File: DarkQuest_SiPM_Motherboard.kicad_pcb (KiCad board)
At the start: 2 copper layers, 100 x 100 mm, 14 parts, among them J1 RJ45_Shielded, J2 SiPM Header, J3 SiPM Header, J4 SiPM Header, J5 SiPM Header

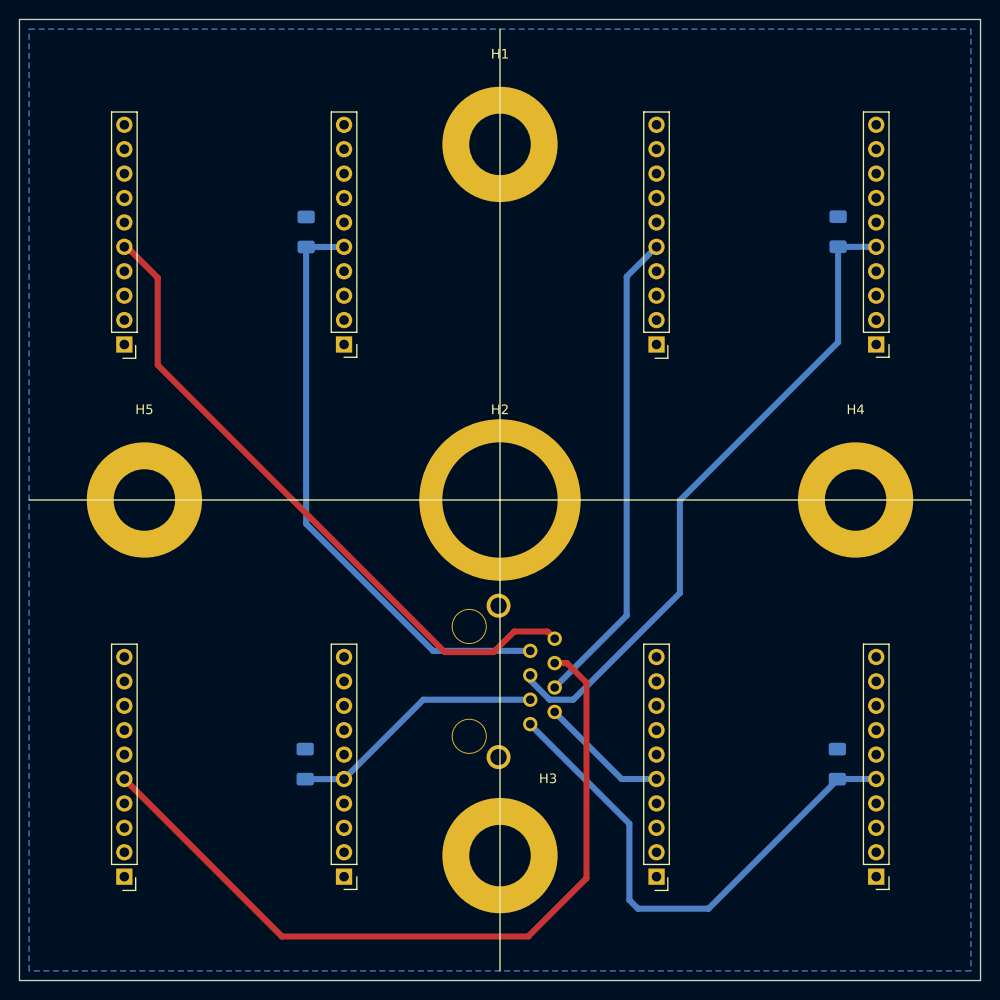
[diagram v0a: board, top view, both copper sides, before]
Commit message: Dual RJ45 Solution
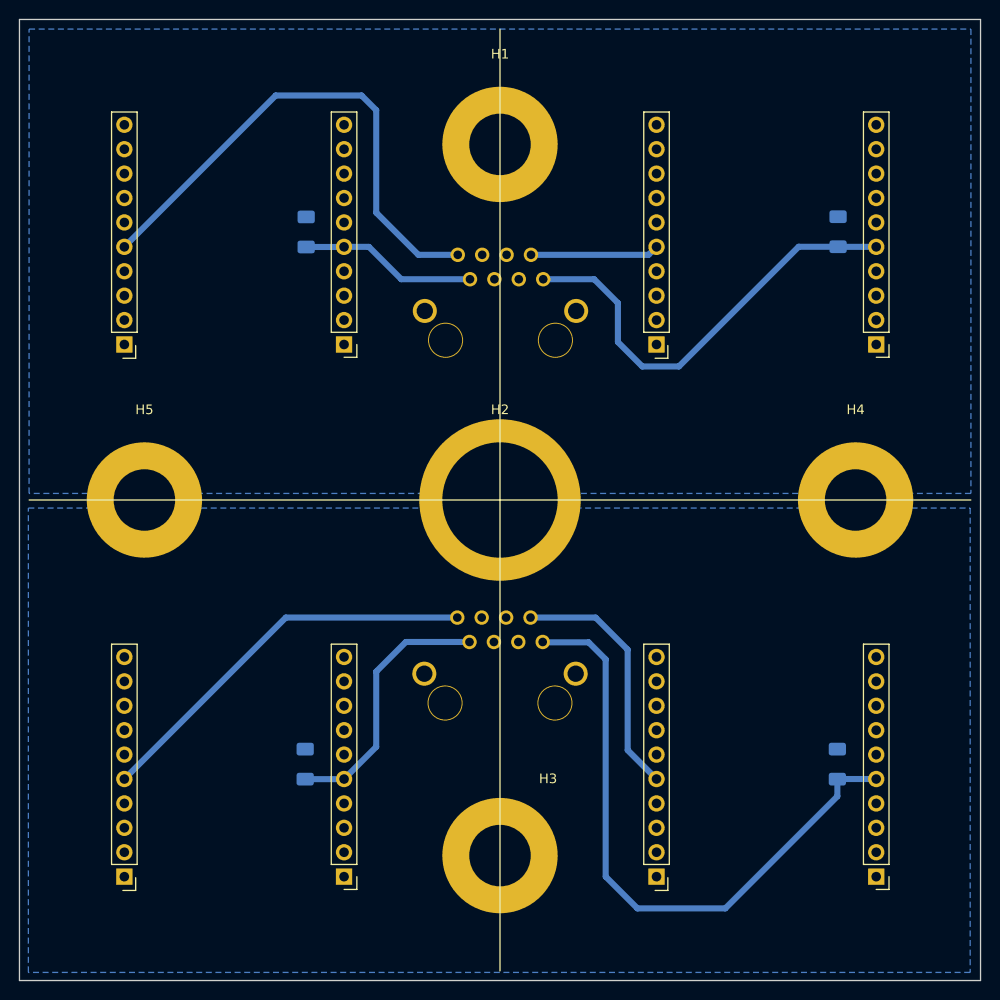
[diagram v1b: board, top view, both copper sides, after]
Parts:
- added J6: RJ45_Shielded, RJJS-88-122-E7V-022:RJJS-88-122-E7V-022, B.Cu at (100.1, 81.2)
- moved J1 1.00 mm to (100.0, 118.9), turned to 180 degrees
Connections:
- C1 pad 2: GND -> GNDA
- C2 pad 2: GND -> GNDA
- C3 pad 2: GND -> GNDB
- C4 pad 2: GND -> GNDB
- J1 pad 3: /K1 -> unconnected-(J1-Pad3)
- J1 pad 4: /A2 -> unconnected-(J1-Pad4)
- J1 pad 5: /K2 -> unconnected-(J1-Pad5)
- J1 pad 6: /A1 -> unconnected-(J1-Pad6)
- J1 pad 7: /K3 -> /K1
- J1 pad 8: /A3 -> /A1
- J1 pad SH: GND -> GNDA
- J2 pad 2: GND -> GNDA
- J3 pad 2: GND -> GNDA
- J4 pad 2: GND -> GNDB
- J5 pad 2: GND -> GNDB
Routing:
- net /K3: track 61.6 -> 18.4 mm
- net /A1: track 81.9 -> 41.6 mm
- net /A2: track 50.2 -> 13.4 mm
- net /K2: track 68.3 -> 45.9 mm
- net /A3: track 68.7 -> 54.3 mm
- net /A0: track 13.5 -> 26.2 mm
- net /K0: track 54.3 -> 66.0 mm
- net /K1: track 26.8 -> 27.6 mm
- added copper zone on B.Cu, net GNDA
- added copper zone on B.Cu, net GNDB
- removed copper zone on B.Cu, net GND
